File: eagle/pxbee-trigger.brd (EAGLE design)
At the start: 75 x 75 mm, 21 parts, among them J1 39501-1002, J2 39501-1009, K1 APAN3103, K2 APAN3103, K3 APAN3103, K4 APAN3103, Q1 BC548BTA, Q2 BC548BTA, Q3 BC548BTA, Q4 BC548BTA

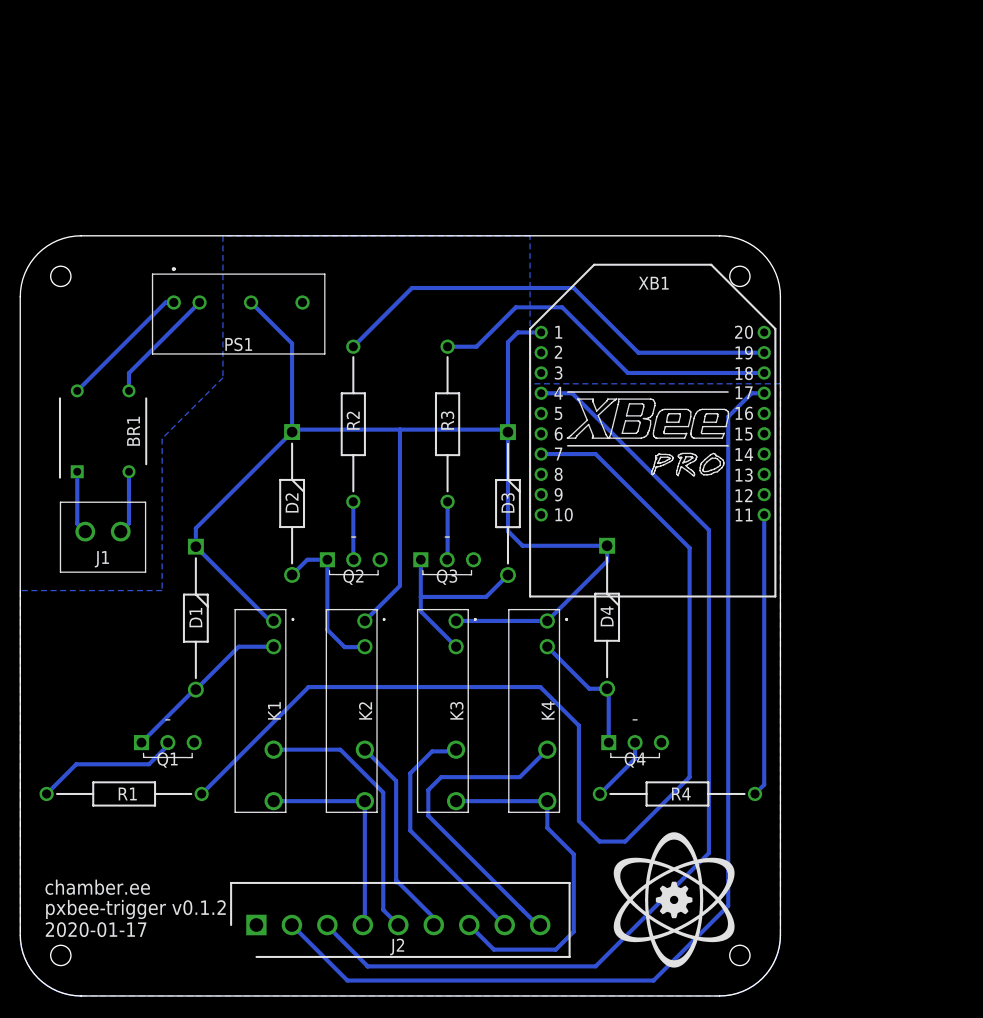
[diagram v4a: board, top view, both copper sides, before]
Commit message: PCB Board changes
- Ready for fabrication v0.1.2-pcbfab.1
- Addresses findings in #5
- New pin assignment from XBee side to accommodate GPIO interrupt usage
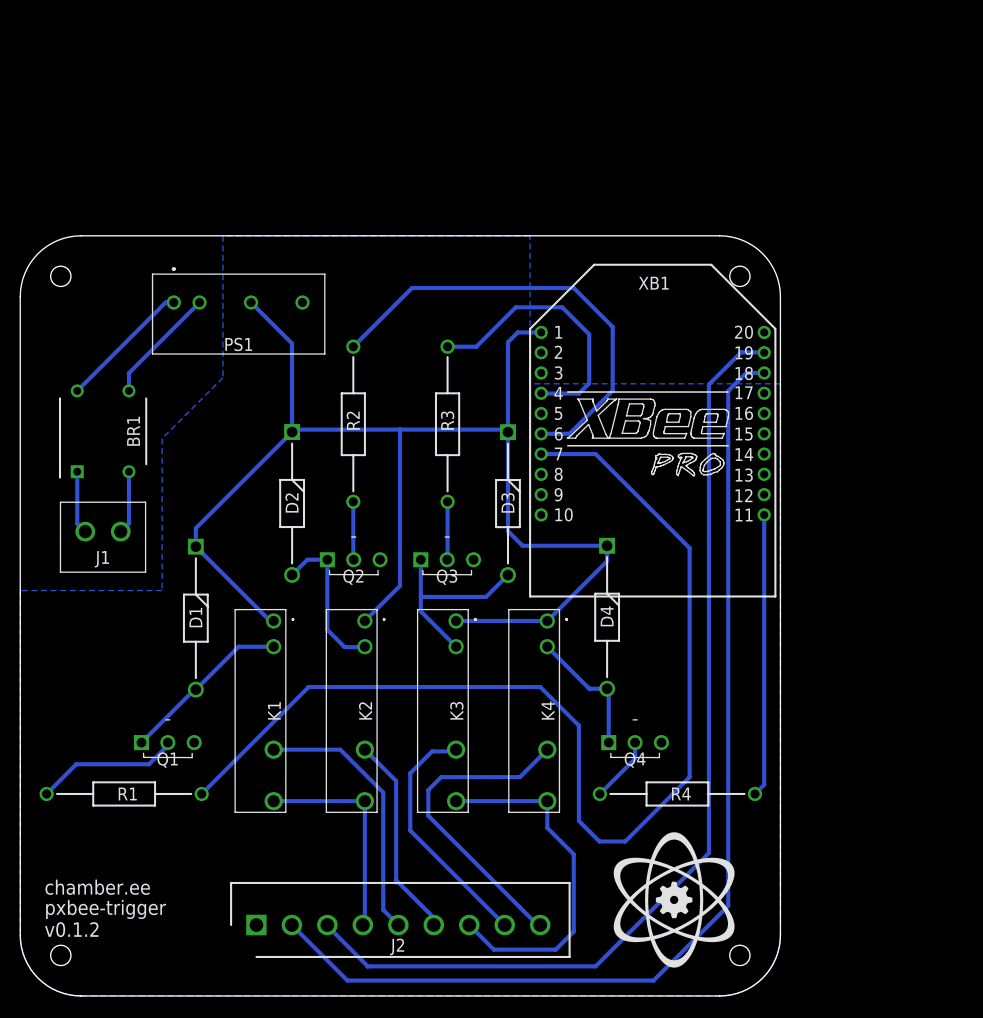
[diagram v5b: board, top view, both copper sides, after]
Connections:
- removed net DIO12: J2.3, XB1.4
- removed net DIO3: J2.2, XB1.17
- new net DIO1: J2.3, XB1.19
- new net DIO2: J2.2, XB1.18
- net N$14: now also XB1.6; no longer XB1.19
- net N$15: now also XB1.4; no longer XB1.18
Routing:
- net DIO2: track 0.00 -> 103.5 mm
- net DIO3: track 101.1 -> 0.00 mm
- net DIO12: track 98.1 -> 0.00 mm
- net DIO1: track 0.00 -> 97.1 mm
- net N$15: track 35.5 -> 26.7 mm
- net N$14: track 45.6 -> 44.7 mm
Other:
- board text added: "pxbee-trigger"
- board text added: "v0.1.2"
- board text removed: "2020-01-17"
- board text removed: "pxbee-trigger v0.1.2"
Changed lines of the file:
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@@
 <wire x1="69" y1="75" x2="6" y2="75" width="0" layer="20"/>
 <text x="2.39" y="10" size="1.4224" layer="21" rot="R180" align="top-right">chamber.ee</text>
-<text x="2.39" y="8" size="1.4224" layer="21" rot="R180" align="top-right">pxbee-trigger v0.1.2</text>
-<text x="2.39" y="5.83455625" size="1.4224" layer="21" rot="R180" align="top-right">2020-01-17</text>
+<text x="2.39" y="8" size="1.4224" layer="21" rot="R180" align="top-right">pxbee-trigger</text>
+<text x="2.39" y="5.83455625" size="1.4224" layer="21" rot="R180" align="top-right">v0.1.2</text>
 <rectangle x1="64.428428125" y1="2.79745625" x2="64.598609375" y2="2.8058375" layer="21"/>
 <rectangle x1="64.344609375" y1="2.8058375" x2="64.682428125" y2="2.81421875" layer="21"/>
@@
 </polygon>
 <contactref element="J2" pad="1"/>
-<wire x1="44.72" y1="43.04" x2="51.4" y2="47.466" width="0" layer="19" extent="1-1"/>
-<wire x1="35.5" y1="43.04" x2="44.72" y2="43.04" width="0" layer="19" extent="1-1"/>
-<wire x1="63.26" y1="25" x2="51.4" y2="47.466" width="0" layer="19" extent="1-1"/>
-<wire x1="17.16" y1="25" x2="35.5" y2="43.04" width="0" layer="19" extent="1-1"/>
-<wire x1="23.3" y1="7" x2="17.16" y2="25" width="0" layer="19" extent="1-1"/>
-<wire x1="27.85" y1="68.42" x2="35.5" y2="43.04" width="0" layer="19" extent="1-1"/>
 </signal>
 <signal name="N$1">
@@
 <signal name="N$14">
 <contactref element="R2" pad="2"/>
-<contactref element="XB1" pad="19"/>
 <wire x1="32.86" y1="64.06" x2="38.65" y2="69.85" width="0.4064" layer="16"/>
 <wire x1="38.65" y1="69.85" x2="54.61" y2="69.85" width="0.4064" layer="16"/>
-<wire x1="60.994" y1="63.466" x2="73.4" y2="63.466" width="0.4064" layer="16"/>
-<wire x1="54.61" y1="69.85" x2="60.994" y2="63.466" width="0.4064" layer="16"/>
+<wire x1="54.61" y1="69.85" x2="58.454" y2="66.006" width="0.4064" layer="16"/>
+<contactref element="XB1" pad="6"/>
+<wire x1="58.454" y1="66.006" x2="58.454" y2="59.724" width="0.4064" layer="16"/>
+<wire x1="58.454" y1="59.724" x2="58.42" y2="59.69" width="0.4064" layer="16"/>
+<wire x1="58.42" y1="59.69" x2="54.196" y2="55.466" width="0.4064" layer="16"/>
+<wire x1="54.196" y1="55.466" x2="51.4" y2="55.466" width="0.4064" layer="16"/>
 </signal>
 <signal name="N$15">
 <contactref element="R3" pad="2"/>
-<contactref element="XB1" pad="18"/>
 <wire x1="42.16" y1="64.06" x2="45.01" y2="64.06" width="0.4064" layer="16"/>
 <wire x1="48.895" y1="67.945" x2="53.467" y2="67.945" width="0.4064" layer="16"/>
 <wire x1="45.01" y1="64.06" x2="48.895" y2="67.945" width="0.4064" layer="16"/>
-<wire x1="73.4" y1="61.466" x2="59.946" y2="61.466" width="0.4064" layer="16"/>
-<wire x1="59.946" y1="61.466" x2="53.467" y2="67.945" width="0.4064" layer="16"/>
+<wire x1="53.467" y1="67.945" x2="56.136" y2="65.276" width="0.4064" layer="16"/>
+<contactref element="XB1" pad="4"/>
+<wire x1="56.136" y1="65.276" x2="56.136" y2="60.454" width="0.4064" layer="16"/>
+<wire x1="56.136" y1="60.454" x2="55.118" y2="59.436" width="0.4064" layer="16"/>
+<wire x1="55.118" y1="59.436" x2="51.43" y2="59.436" width="0.4064" layer="16"/>
+<wire x1="51.43" y1="59.436" x2="51.4" y2="59.466" width="0.4064" layer="16"/>
 </signal>
 <signal name="N$16">
@@
 <wire x1="10.724" y1="46.623" x2="9.914" y2="45.813" width="0.4064" layer="16"/>
 </signal>
-<signal name="DIO12">
-<contactref element="XB1" pad="4"/>
+<signal name="DIO2">
+<contactref element="XB1" pad="18"/>
+<contactref element="J2" pad="2"/>
+<wire x1="26.8" y1="7" x2="32.276" y2="1.524" width="0.4064" layer="16"/>
+<wire x1="32.276" y1="1.524" x2="62.484" y2="1.524" width="0.4064" layer="16"/>
+<wire x1="62.484" y1="1.524" x2="69.85" y2="8.89" width="0.4064" layer="16"/>
+<wire x1="69.85" y1="59.69" x2="71.628" y2="61.468" width="0.4064" layer="16"/>
+<wire x1="71.628" y1="61.468" x2="73.398" y2="61.468" width="0.4064" layer="16"/>
+<wire x1="73.398" y1="61.468" x2="73.4" y2="61.466" width="0.4064" layer="16"/>
+<wire x1="69.85" y1="8.89" x2="69.85" y2="59.69" width="0.4064" layer="16"/>
+</signal>
+<signal name="DIO1">
+<contactref element="XB1" pad="19"/>
 <wire x1="34.214" y1="2.921" x2="34.29" y2="2.921" width="0.4064" layer="16"/>
 <wire x1="34.29" y1="2.921" x2="56.769" y2="2.921" width="0.4064" layer="16"/>
 <wire x1="56.769" y1="2.921" x2="67.945" y2="14.097" width="0.4064" layer="16"/>
-<wire x1="54.453" y1="59.466" x2="51.4" y2="59.466" width="0.4064" layer="16"/>
-<wire x1="67.945" y1="14.097" x2="67.945" y2="45.974" width="0.4064" layer="16"/>
-<wire x1="67.945" y1="45.974" x2="54.453" y2="59.466" width="0.4064" layer="16"/>
+<wire x1="67.945" y1="14.097" x2="67.945" y2="45.72" width="0.4064" layer="16"/>
 <contactref element="J2" pad="3"/>
+<wire x1="67.945" y1="45.72" x2="67.945" y2="45.974" width="0.4064" layer="16"/>
 <wire x1="34.29" y1="2.921" x2="30.3" y2="6.911" width="0.4064" layer="16"/>
 <wire x1="30.3" y1="6.911" x2="30.3" y2="7" width="0.4064" layer="16"/>
-</signal>
-<signal name="DIO3">
-<contactref element="J2" pad="2"/>
-<contactref element="XB1" pad="17"/>
-<wire x1="26.8" y1="7" x2="32.276" y2="1.524" width="0.4064" layer="16"/>
-<wire x1="32.276" y1="1.524" x2="62.484" y2="1.524" width="0.4064" layer="16"/>
-<wire x1="62.484" y1="1.524" x2="69.85" y2="8.89" width="0.4064" layer="16"/>
-<wire x1="69.85" y1="8.89" x2="69.85" y2="57.15" width="0.4064" layer="16"/>
-<wire x1="69.85" y1="57.15" x2="72.166" y2="59.466" width="0.4064" layer="16"/>
-<wire x1="72.166" y1="59.466" x2="73.4" y2="59.466" width="0.4064" layer="16"/>
+<wire x1="67.945" y1="45.974" x2="67.945" y2="60.325" width="0.4064" layer="16"/>
+<wire x1="67.945" y1="60.325" x2="71.12" y2="63.5" width="0.4064" layer="16"/>
+<wire x1="71.12" y1="63.5" x2="73.366" y2="63.5" width="0.4064" layer="16"/>
+<wire x1="73.366" y1="63.5" x2="73.4" y2="63.466" width="0.4064" layer="16"/>
 </signal>
 </signals>

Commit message: Shrinking the pcb design to 51x64mm
- Addressing findings in #6
- Eagle upgrade to 9.6.0
- WIP
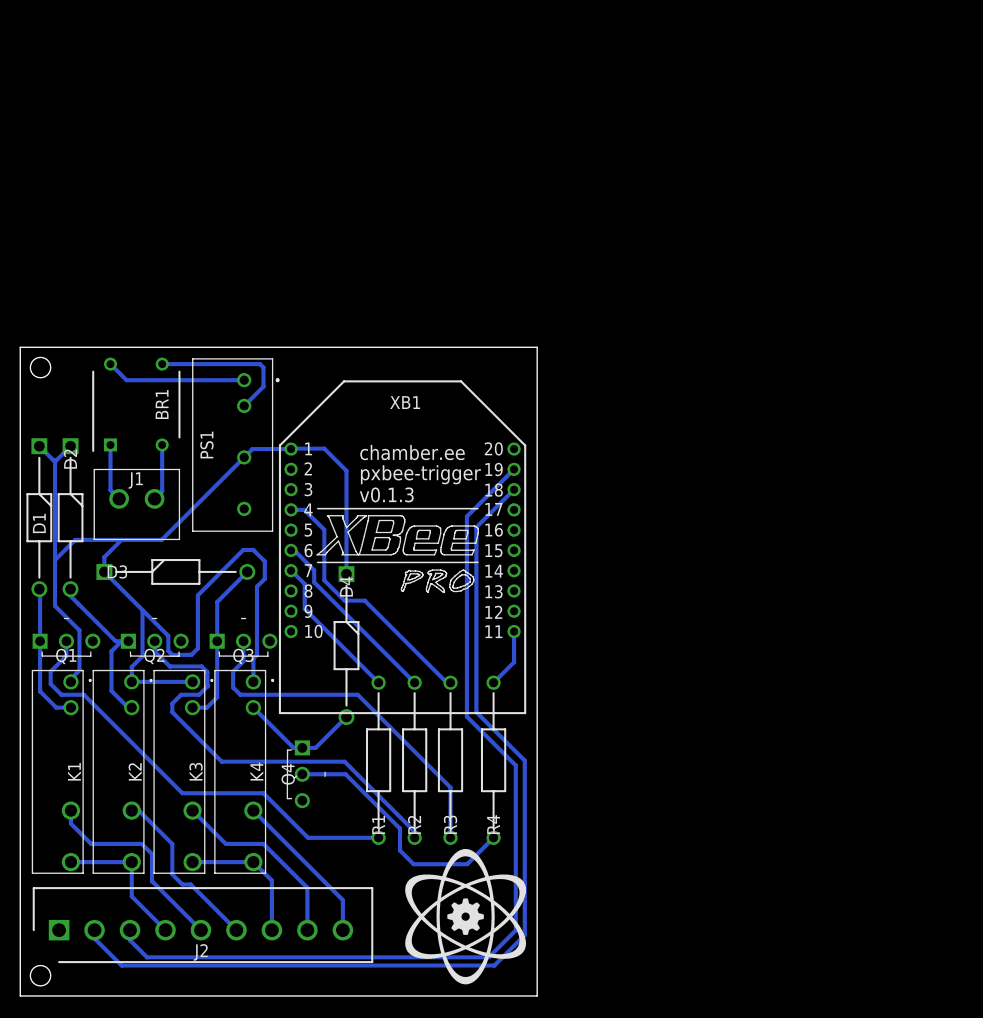
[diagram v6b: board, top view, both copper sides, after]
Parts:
- moved D3 42.1 mm to (8.30, 41.8), turned to 0 degrees
- moved R2 33.7 mm to (38.9, 15.6)
- moved R3 33.2 mm to (42.5, 15.6)
- moved R1 33.0 mm to (35.4, 15.6), turned to 90 degrees
- moved Q4 30.2 mm to (27.8, 24.5), turned to 270 degrees
- moved K4 29.6 mm to (23.0, 31.0)
- moved XB1 27.2 mm to (37.7, 45.2)
- moved K3 26.7 mm to (17.0, 31.0)
- moved D4 25.9 mm to (32.2, 41.6)
- moved K2 23.8 mm to (11.0, 31.0)
- moved D2 21.9 mm to (4.96, 54.2)
- moved Q3 21.6 mm to (19.4, 35.0)
- moved Q2 21.2 mm to (10.7, 35.0)
- moved K1 20.9 mm to (5.00, 31.0)
- moved J2 19.5 mm to (3.83, 6.49)
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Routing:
- net N$13: track 108.0 -> 14.6 mm
- net N$2: track 5.74 -> 43.0 mm
- net N$5: track 5.74 -> 35.5 mm
- net N$1: track 14.2 -> 43.5 mm
- net N$14: track 44.7 -> 18.3 mm
- net N$16: track 27.9 -> 5.89 mm
- net COM2: track 35.0 -> 13.5 mm
- net N$7: track 6.51 -> 24.9 mm
- net ACT4: track 31.4 -> 15.5 mm
- net DIO2: track 103.5 -> 93.1 mm
- net COM1: track 21.3 -> 14.1 mm
- net DIO1: track 97.1 -> 90.3 mm
- net ACT1: track 26.2 -> 20.0 mm
- net ACT3: track 24.3 -> 18.7 mm
- net VCC: track 133.7 -> 129.5 mm
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- removed copper zone on layer 16, net GND
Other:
- board size 75 x 75 mm -> 51 x 64 mm
- board text added: "v0.1.3"
- board text removed: "v0.1.2"

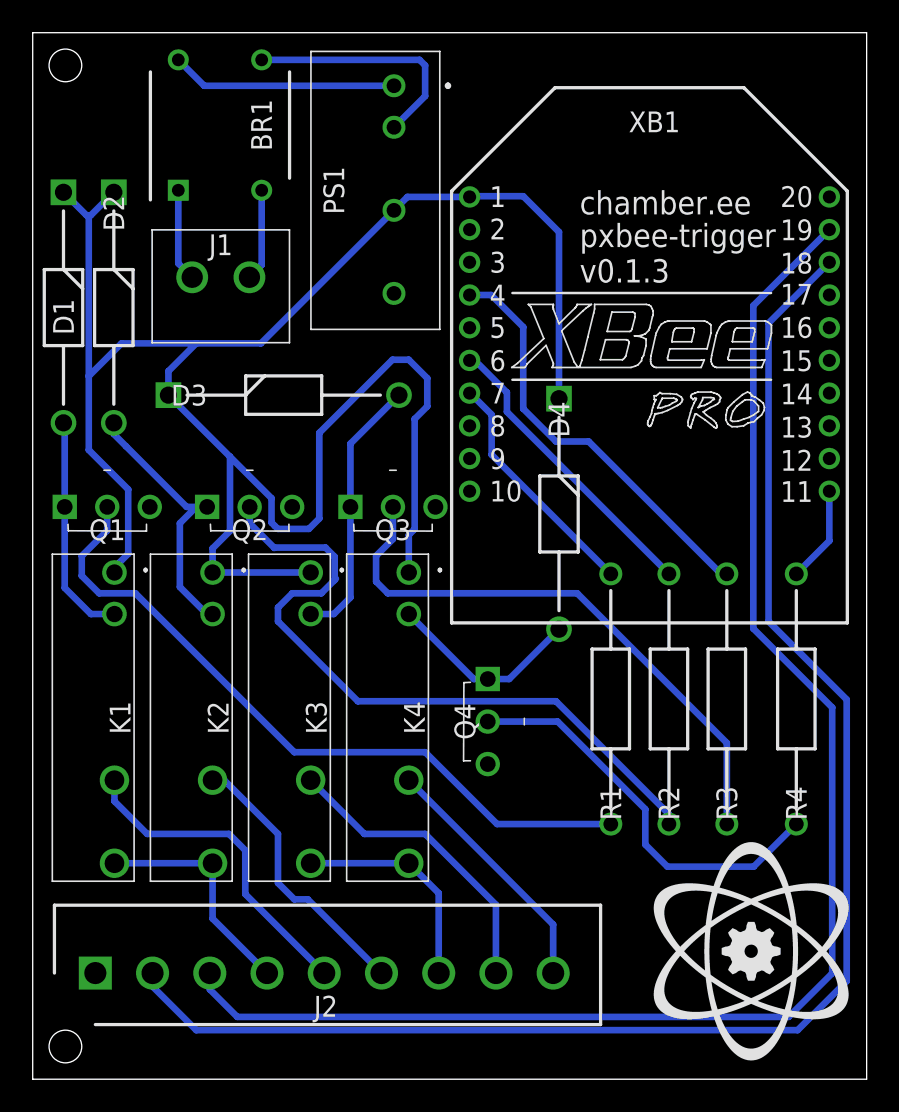
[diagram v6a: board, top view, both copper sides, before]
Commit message: Further shrinkin the pcb size, new format: 51x57mm
- Addresses findings in #6
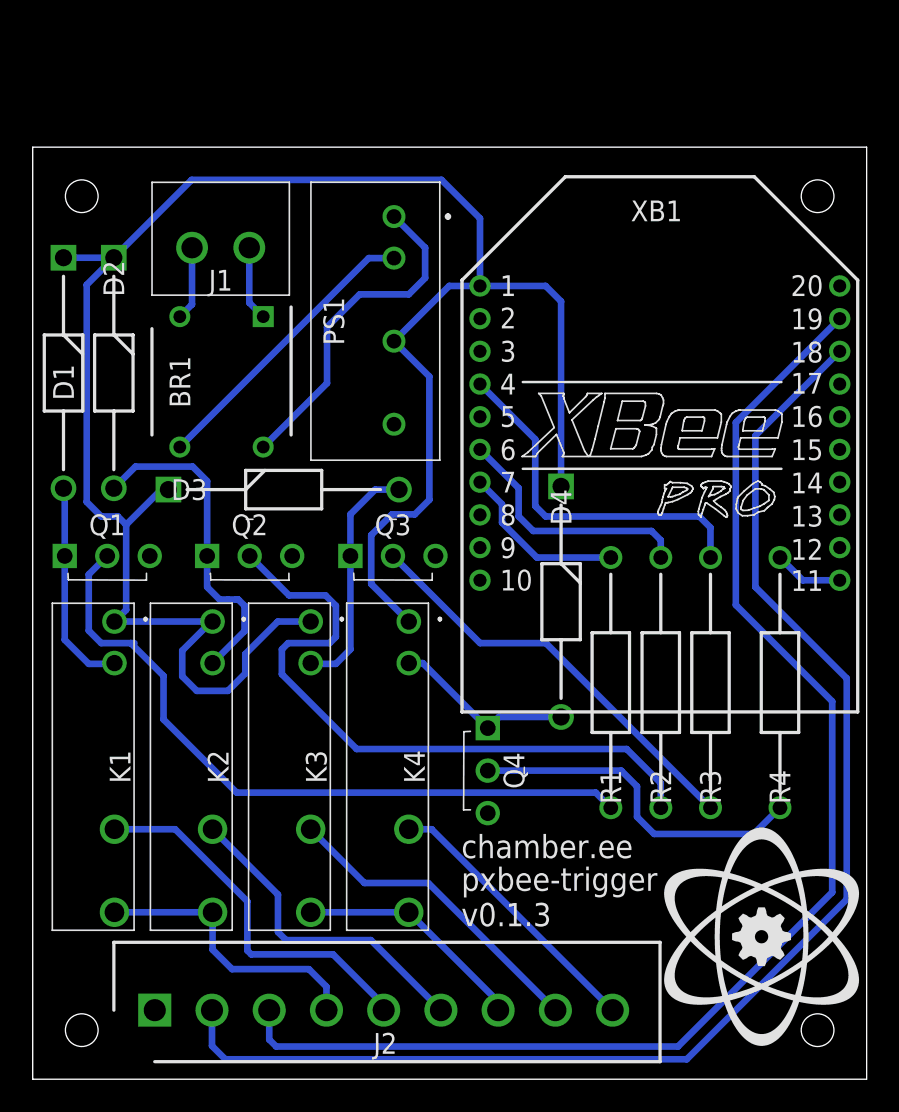
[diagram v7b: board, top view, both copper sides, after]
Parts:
- moved BR1 15.7 mm to (11.5, 42.6), turned to 270 degrees
- moved PS1 8.00 mm to (21.0, 46.4)
- moved D3 5.78 mm to (8.30, 36.1)
- moved XB1 5.48 mm to (38.4, 39.8)
- moved D4 5.37 mm to (32.3, 36.3)
- moved J2 4.29 mm to (7.46, 4.22)
- moved D1 4.00 mm to (1.88, 50.2)
- moved D2 4.00 mm to (4.96, 50.2)
- moved J1 3.95 mm to (9.75, 50.9), turned to 0 degrees
- moved K1 3.00 mm to (5.00, 28.0)
- moved K2 3.00 mm to (11.0, 28.0)
- moved K3 3.00 mm to (17.0, 28.0)
- moved K4 3.00 mm to (23.0, 28.0)
- moved Q1 3.00 mm to (1.96, 32.0)
- moved Q2 3.00 mm to (10.7, 32.0)
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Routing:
- net DIO1: track 90.3 -> 80.5 mm
- net DIO2: track 93.1 -> 83.4 mm
- net N$5: track 35.5 -> 25.8 mm
- net N$10: track 13.8 -> 20.7 mm
- net N$13: track 14.6 -> 10.6 mm
- net N$15: track 25.7 -> 22.0 mm
- net N$7: track 24.9 -> 21.2 mm
- net COM1: track 14.1 -> 17.6 mm
- net VCC: track 129.5 -> 126.2 mm
- net N$4: track 16.9 -> 20.2 mm
- net N$11: track 14.7 -> 17.9 mm
- net ACT1: track 20.0 -> 23.0 mm
- net ACT2: track 17.0 -> 19.9 mm
- net N$14: track 18.3 -> 15.4 mm
- net N$2: track 43.0 -> 41.0 mm
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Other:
- board size 51 x 64 mm -> 51 x 57 mm
